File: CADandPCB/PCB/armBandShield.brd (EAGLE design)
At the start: 22.5 x 54.6 mm, 25 parts, among them U1 MPU-9250

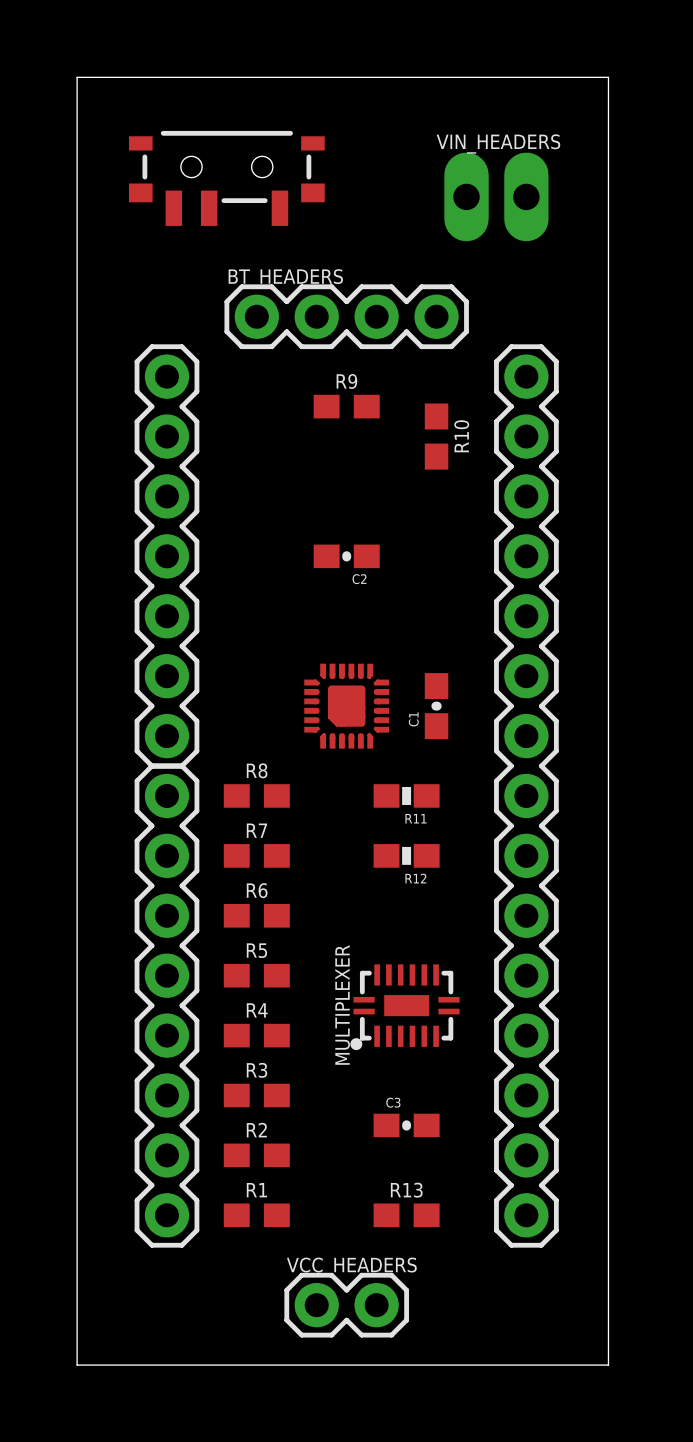
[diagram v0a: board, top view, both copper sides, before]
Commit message: Clean up silk screen and add ground plane.
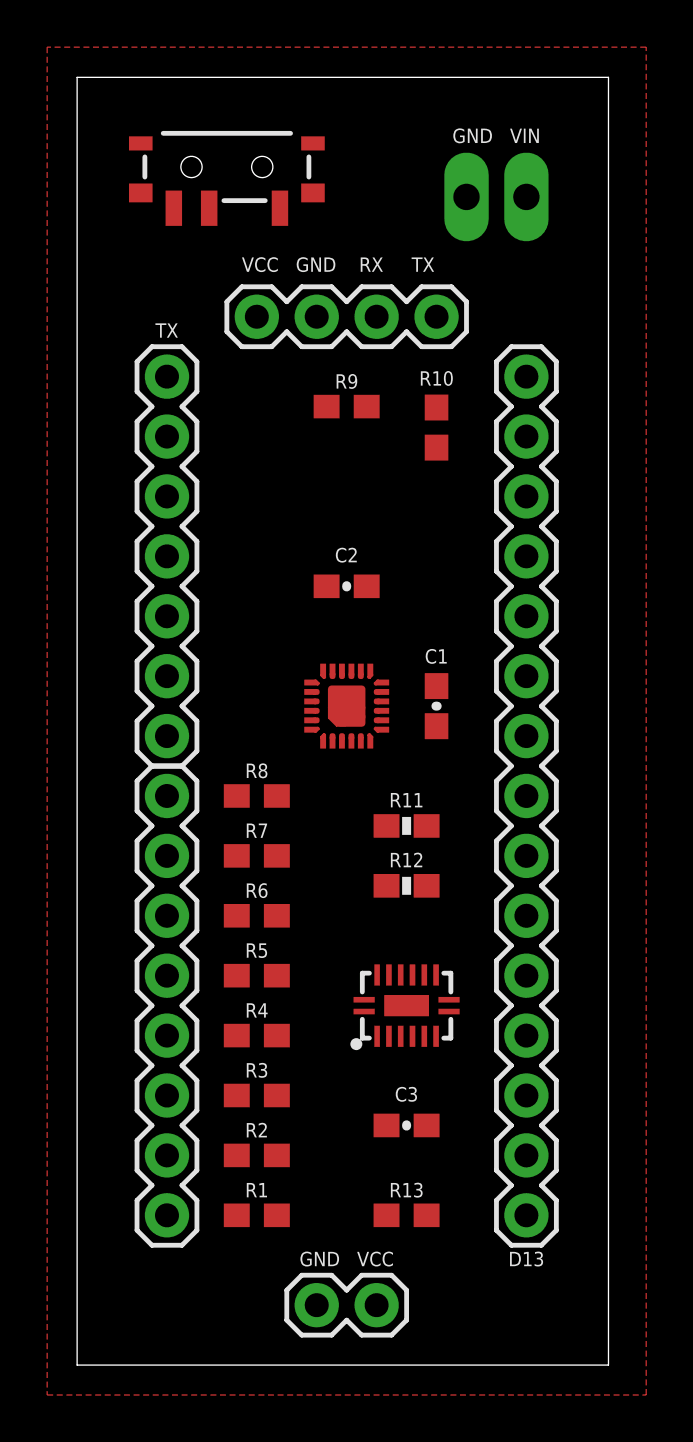
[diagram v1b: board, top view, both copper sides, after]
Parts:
- moved R11 1.27 mm to (14.0, 22.9)
- moved R12 1.27 mm to (14.0, 20.3)
- moved C2 1.27 mm to (11.4, 33.0)
- moved R10 0.38 mm to (15.2, 39.8)
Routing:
- added copper zone on layer 1, net GND
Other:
- board text added: "C2"
- board text added: "D13"
- board text added: "GND VCC"
- board text added: "GND VIN"
- board text added: "TX"
- board text added: "VCC GND RX TX"

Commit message: All connections routed
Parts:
- moved C1 5.39 mm to (11.4, 31.8), turned to 0 degrees
- moved R13 4.49 mm to (14.6, 10.8), turned to 270 degrees
- moved C2 4.20 mm to (7.62, 31.2), turned to 90 degrees
- moved R12 3.24 mm to (13.3, 23.5), turned to 270 degrees
- moved C3 3.24 mm to (14.6, 6.99), turned to 90 degrees
- moved R11 1.42 mm to (15.2, 23.5), turned to 270 degrees
- moved R8 1.09 mm to (6.73, 24.8), turned to 270 degrees
- moved MULTIPLEXER 0.38 mm to (13.6, 15.2)
- turned U1 to 180 degrees
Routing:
- net VCC: track 0.00 -> 61.8 mm, vias 0 -> 2
- net VCC_2: track 0.00 -> 47.8 mm, vias 0 -> 2
- net D2: track 0.00 -> 19.6 mm, vias 0 -> 1
- net D4: track 0.00 -> 18.4 mm, vias 0 -> 1
- net D3: track 0.00 -> 18.0 mm, vias 0 -> 1
- net FSR5: track 0.00 -> 17.1 mm, vias 0 -> 1
- net VIN: track 0.00 -> 17.0 mm
- net FSR1: track 0.00 -> 16.4 mm, vias 0 -> 1
- net FSR8: track 0.00 -> 15.9 mm
- net FSR2: track 0.00 -> 13.6 mm, vias 0 -> 1
- net A4/SDA: track 0.00 -> 13.6 mm, vias 0 -> 2
- net FSR3: track 0.00 -> 13.2 mm
- net FSR7: track 0.00 -> 11.8 mm
- net GND: track 0.00 -> 11.6 mm
- net RX: track 0.00 -> 11.0 mm
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- added copper zone on layer 16, net GND
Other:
- board size 22.5 x 54.6 mm -> 22.9 x 54.6 mm
- board text added: "BOURK AND RICO V1.0"
- board text added: "VIN GND"
- board text removed: "GND VIN"

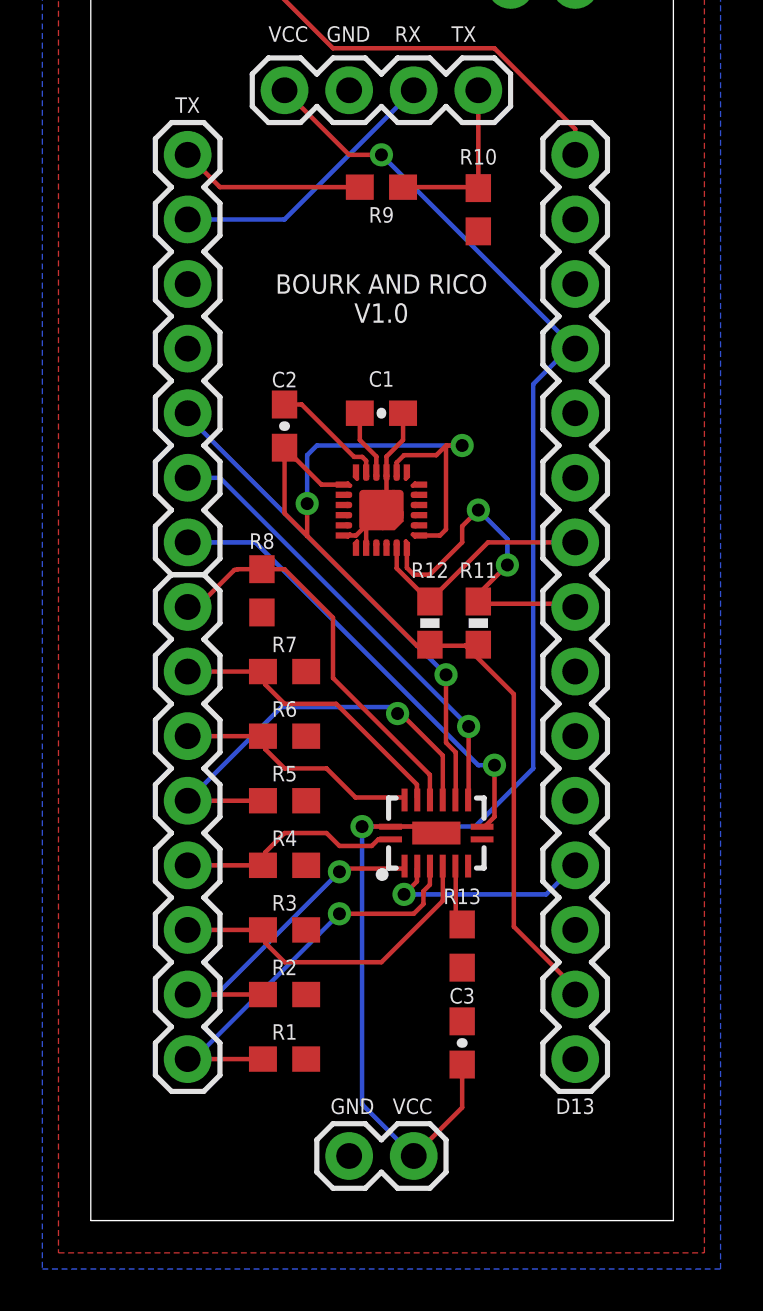
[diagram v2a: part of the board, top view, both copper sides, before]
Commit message: Increase solder pad lengths for chips
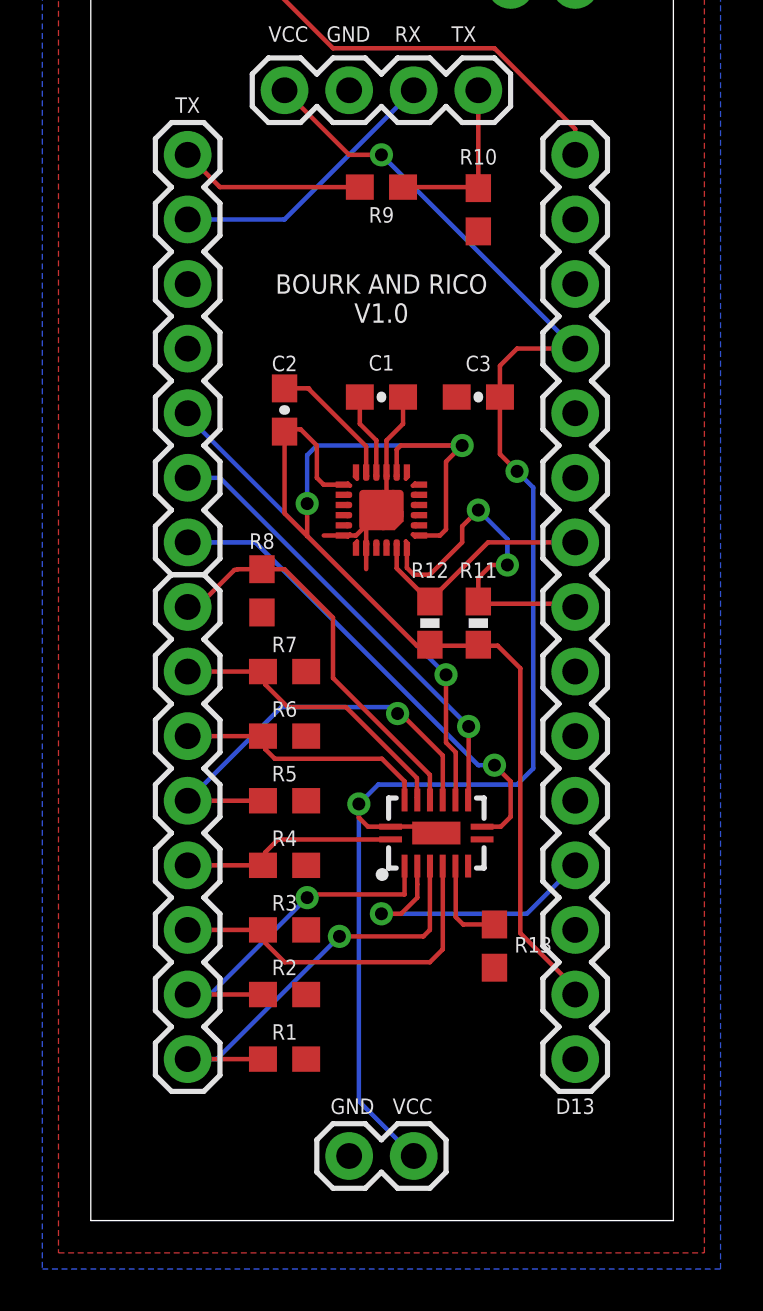
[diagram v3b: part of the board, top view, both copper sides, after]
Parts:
- moved C3 25.4 mm to (15.2, 32.4), turned to 180 degrees
- moved R13 1.27 mm to (15.9, 10.8)
- moved C1 0.63 mm to (11.4, 32.4)
- moved C2 0.63 mm to (7.62, 31.9)
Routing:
- net A0: track 8.53 -> 11.3 mm
- net GND: track 11.6 -> 14.4 mm
- net VCC_2: track 47.8 -> 50.5 mm
- net N$2: track 2.40 -> 3.65 mm
- net FSR3: track 13.2 -> 14.3 mm
- net D4: track 18.4 -> 19.3 mm
- net FSR1: track 16.4 -> 17.1 mm
- net REGOUT: track 2.53 -> 3.16 mm
- net FSR2: track 13.6 -> 14.2 mm
- net VCC: track 61.8 -> 61.3 mm, vias 2 -> 3

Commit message: Begin performing DRC checks
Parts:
- moved R13 3.30 mm to (15.0, 7.62), turned to 0 degrees
- moved R1 0.63 mm to (6.99, 6.35)
- moved R2 0.63 mm to (6.99, 8.89)
- moved R3 0.63 mm to (6.99, 11.4)
- moved R4 0.63 mm to (6.99, 14.0)
- moved R5 0.63 mm to (6.99, 16.5)
- moved R6 0.63 mm to (6.99, 19.1)
- moved R7 0.63 mm to (6.99, 21.6)
- moved R12 0.13 mm to (13.2, 23.5)
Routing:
- net N$2: track 3.65 -> 6.41 mm
- net FSR3: track 14.3 -> 15.6 mm
- net FSR2: track 14.2 -> 13.5 mm
- net D3: track 18.0 -> 18.7 mm
- net FSR5: track 17.1 -> 16.4 mm
- net FSR1: track 17.1 -> 16.5 mm
- net VCC_2: track 50.5 -> 51.1 mm
- net FSR8: track 15.9 -> 15.3 mm
- net GND: track 14.4 -> 14.3 mm, vias 0 -> 5

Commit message: Rev 1 board completed. Performed checks and added headers for switch.
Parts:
- removed VIN_SWITCH: (no value), SparkFun-Switches:SWITCH_SPST_SMD_A
- added SWITCH_HEADERS: 455-1750-1-ND, SparkFun-Connectors:1X03
- moved VIN_HEADERS 12.7 mm to (3.81, 50.2)
- moved R8 0.28 mm to (6.99, 24.9)
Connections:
- net N$1: now also SWITCH_HEADERS.2; no longer VIN_SWITCH.3
- net VIN: now also SWITCH_HEADERS.1; no longer VIN_SWITCH.2
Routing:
- net VIN: track 17.0 -> 8.26 mm
- net N$1: track 8.45 -> 16.6 mm
- net FSR1: track 16.5 -> 18.8 mm
- net FSR2: track 13.5 -> 15.4 mm
- net VCC: track 61.3 -> 62.8 mm
- net FSR4: track 8.70 -> 9.26 mm
- net FSR6: track 10.00 -> 10.5 mm
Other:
- board text added: "OFF ON"

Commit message: Replace MPU-9250 with MPU-6050. Added logic level. Cleaned up schematic.
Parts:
- removed C1, C2: 0.1uF, SparkFun-Capacitors:0603-CAP
- removed R11, R12: 10K, SparkFun-Resistors:0603-RES
- removed R13: 10k, SparkFun-Resistors:0603
- removed U1: MPU-9250, Testing:QFN24_PAD
- added C4, C7: 0.1uF, SparkFun-Capacitors:0603-CAP
- added C5: 10nF, SparkFun-Capacitors:0603
- added C6: 2.2nF, SparkFun-Capacitors:0603
- added IMU: MPU-6050-1, Testing:QFN-24-4MM2
- added LLC1, LLC2: BSS138, SparkFun:SOT23-3
- added R16, R17, R20, R21: 10K, SparkFun:0603-RES
- added R18, R19: 10K, SparkFun-Resistors:0603-RES
- MULTIPLEXER: value (none) -> 74HC4051
- renumbered MULTIPLEXER_HEADERS to FSR_HEADERS
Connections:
- removed net A4/SDA: R11.1, RIGHT_HEADER.8, U1.24
- removed net A5/SCL: R12.1, RIGHT_HEADER.9, U1.23
- removed net N$2: MULTIPLEXER.6, R13.1
- removed net REGOUT: C1.1, U1.10
- new net A4/SDA/HIGH: LLC1.3, R17.2, RIGHT_HEADER.8
- new net A4/SDA/LOW: IMU.24, LLC1.2, R16.2, R18.2
- new net A5/SCL/HIGH: LLC2.3, R21.2, RIGHT_HEADER.9
- new net A5/SCL/LOW: IMU.23, LLC2.2, R19.2, R20.2
- new net N$3: C6.1, IMU.20
- new net N$5: C4.1, IMU.10
- net GND: now also C4.2, C5.2, C6.2, C7.2, IMU.1, IMU.11, IMU.18, IMU.9, MULTIPLEXER.6; no longer C1.2, C2.2, R13.2, U1.11, U1.18, U1.20, U1.9, U1.CENTER
- net VCC: now also R17.1, R21.1
- net VCC_2: now also C5.1, C7.1, IMU.13, IMU.8, LLC1.1, LLC2.1, R16.1, R18.1, R19.1, R20.1; no longer C2.1, R11.2, R12.2, U1.1, U1.13, U1.8
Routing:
- net A4/SDA: track 13.9 -> 0.00 mm, vias 2 -> 0
- net A5/SCL: track 9.34 -> 0.00 mm
- net VCC_2: track 51.1 -> 41.8 mm
- net GND: track 14.3 -> 6.11 mm
- net N$2: track 6.41 -> 0.00 mm
- net REGOUT: track 3.16 -> 0.00 mm

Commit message: Initial layout 95% complete
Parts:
- removed FSR_HEADERS: (no value), SparkFun-Connectors:1X08
- removed IMU: MPU-6050-1, Testing:QFN-24-4MM2
- removed LLC1, LLC2: BSS138, SparkFun:SOT23-3
- removed MULTIPLEXER: 74HC4051, SparkFun-IC-Logic:DHVQFN-16-2.5X3.5MM
- added 74HC4051: U1, SparkFun-IC-Logic:DHVQFN-16-2.5X3.5MM
- added J1: FSR_HEADERS_1, SparkFun-Connectors:1X04
- added J2: FSR_HEADERS_2, SparkFun-Connectors:1X04
- added Q1, Q2: BSS138, SparkFun:SOT23-3
- added U2: MPU-6050-1, Testing:QFN-24-4MM2
- BT_HEADERS: value (none) -> J5; device SparkFun-Connectors:1X04@1 -> SparkFun-Connectors:1X04
- LEFT_HEADER: value (none) -> J3
- RIGHT_HEADER: value (none) -> J4; device SparkFun-Connectors:1X15 -> SparkFun-Connectors:1X14
- SWITCH_HEADERS: value 455-1750-1-ND -> J8
- VCC_HEADERS: value (none) -> J6; device SparkFun-Connectors:1X02 -> SparkFun-Connectors:1X02_LONGPADS
- VIN_HEADERS: value (none) -> J7
- moved C7 60.3 mm to (8.89, 32.4), turned to 270 degrees
- moved R20 58.1 mm to (10.8, 23.4), turned to 180 degrees
- moved R21 57.2 mm to (10.8, 16.5), turned to 90 degrees
- moved C4 56.5 mm to (10.2, 37.5), turned to 180 degrees
- moved R19 56.3 mm to (10.8, 25.7)
- moved C6 55.9 mm to (10.8, 27.9), turned to 180 degrees
- moved R18 51.6 mm to (15.2, 25.7), turned to 180 degrees
- moved C5 42.9 mm to (15.9, 37.5), turned to 180 degrees
- moved R16 32.0 mm to (15.2, 23.4), turned to 180 degrees
- moved R17 31.8 mm to (15.2, 16.5), turned to 90 degrees
- moved R8 19.2 mm to (2.03, 6.35)
- moved R1 18.3 mm to (25.3, 6.35), turned to 90 degrees
- moved C3 16.3 mm to (5.08, 19.7)
- moved R2 16.0 mm to (22.7, 6.35), turned to 90 degrees
- moved R7 15.4 mm to (4.57, 6.35), turned to 90 degrees
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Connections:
- net A0: now also 74HC4051.3, RIGHT_HEADER.3; no longer MULTIPLEXER.3, RIGHT_HEADER.4
- net A4/SDA/HIGH: now also Q1.3, RIGHT_HEADER.7; no longer LLC1.3, RIGHT_HEADER.8
- net A4/SDA/LOW: now also Q1.2, U2.24; no longer IMU.24, LLC1.2
- net A5/SCL/HIGH: now also Q2.3, RIGHT_HEADER.8; no longer LLC2.3, RIGHT_HEADER.9
- net A5/SCL/LOW: now also Q2.2, U2.23; no longer IMU.23, LLC2.2
- net D2: now also 74HC4051.11; no longer MULTIPLEXER.11
- net D3: now also 74HC4051.10; no longer MULTIPLEXER.10
- net D4: now also 74HC4051.9; no longer MULTIPLEXER.9
- net FSR1: now also 74HC4051.4, J2.1; no longer FSR_HEADERS.1, MULTIPLEXER.4
- net FSR2: now also 74HC4051.2, J2.2; no longer FSR_HEADERS.2, MULTIPLEXER.2
- net FSR3: now also 74HC4051.5, J2.3; no longer FSR_HEADERS.3, MULTIPLEXER.5
- net FSR4: now also 74HC4051.1, J2.4; no longer FSR_HEADERS.4, MULTIPLEXER.1
- net FSR5: now also 74HC4051.12, J1.1; no longer FSR_HEADERS.5, MULTIPLEXER.12
- net FSR6: now also 74HC4051.15, J1.2; no longer FSR_HEADERS.6, MULTIPLEXER.15
- net FSR7: now also 74HC4051.14, J1.3; no longer FSR_HEADERS.7, MULTIPLEXER.14
- net FSR8: now also 74HC4051.13, J1.4; no longer FSR_HEADERS.8, MULTIPLEXER.13
- net GND: now also 74HC4051.6, 74HC4051.7, 74HC4051.8, RIGHT_HEADER.13, U2.1, U2.11, U2.18, U2.9; no longer IMU.1, IMU.11, IMU.18, IMU.9, MULTIPLEXER.6, MULTIPLEXER.7, MULTIPLEXER.8, RIGHT_HEADER.14
- net N$3: now also U2.20; no longer IMU.20
- net N$5: now also U2.10; no longer IMU.10
- net VCC: now also 74HC4051.16, 74HC4051.EP, RIGHT_HEADER.11; no longer MULTIPLEXER.16, MULTIPLEXER.EP, RIGHT_HEADER.12
- net VCC_2: now also Q1.1, Q2.1, RIGHT_HEADER.1, U2.13, U2.8; no longer IMU.13, IMU.8, LLC1.1, LLC2.1, RIGHT_HEADER.2
- net VIN: now also RIGHT_HEADER.14; no longer RIGHT_HEADER.15
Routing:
- net VCC: track 62.8 -> 105.9 mm, vias 3 -> 0
- net VCC_2: track 41.8 -> 71.7 mm, vias 2 -> 0
- net D2: track 19.6 -> 0.00 mm, vias 1 -> 0
- net A5/SCL/HIGH: track 0.00 -> 18.8 mm
- net A4/SDA/HIGH: track 0.00 -> 12.1 mm
- net A0: track 11.3 -> 0.00 mm, vias 1 -> 0
- net A5/SCL/LOW: track 0.00 -> 10.8 mm
- net FSR8: track 15.7 -> 5.32 mm
- net A4/SDA/LOW: track 0.00 -> 9.27 mm
- net FSR1: track 18.8 -> 27.0 mm
- net FSR2: track 15.4 -> 22.8 mm, vias 1 -> 0
- net FSR3: track 15.9 -> 22.5 mm, vias 0 -> 1
- net FSR4: track 9.26 -> 2.99 mm
- net GND: track 6.11 -> 0.00 mm, vias 5 -> 0
- net D4: track 19.3 -> 14.6 mm, vias 1 -> 0
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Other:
- board size 22.9 x 54.6 mm -> 27.4 x 55.9 mm
- board text added: "3.3 V"
- board text added: "RX"
- board text removed: "C2"

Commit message: Board V2 Completed.
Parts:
- moved C7 8.28 mm to (13.3, 39.4), turned to 0 degrees
- moved 74HC4051 7.80 mm to (12.1, 10.7)
- moved J1 6.48 mm to (3.17, 2.41), turned to 90 degrees
- moved R8 5.68 mm to (6.35, 10.0), turned to 0 degrees
- moved R5 5.14 mm to (6.35, 2.41), turned to 0 degrees
- moved VCC_HEADERS 2.29 mm to (10.2, 2.92)
- moved R7 2.11 mm to (6.35, 7.49), turned to 0 degrees
- moved C3 2.01 mm to (5.71, 21.6)
- moved R6 1.59 mm to (6.35, 4.95), turned to 0 degrees
- moved R3 1.27 mm to (18.9, 6.35)
- moved C5 1.27 mm to (17.1, 37.5), turned to 0 degrees
- moved J2 1.27 mm to (24.0, 2.54)
- moved R1 1.27 mm to (24.0, 6.35)
- moved R2 1.27 mm to (21.5, 6.35)
- moved R4 1.27 mm to (16.4, 6.35)
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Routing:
- net D2: track 0.00 -> 28.4 mm
- net VCC: track 105.9 -> 88.4 mm, vias 0 -> 1
- net GND: track 0.00 -> 14.1 mm, vias 0 -> 5
- net A0: track 0.00 -> 11.9 mm, vias 0 -> 1
- net FSR1: track 27.0 -> 17.0 mm, vias 1 -> 0
- net FSR2: track 22.8 -> 13.1 mm
- net D4: track 14.6 -> 21.9 mm
- net D3: track 17.7 -> 24.8 mm
- net FSR4: track 2.99 -> 9.78 mm
- net RX: track 12.9 -> 18.1 mm
- net FSR7: track 12.6 -> 8.59 mm
- net FSR3: track 22.5 -> 18.5 mm
- net VCC_2: track 71.7 -> 75.6 mm, vias 0 -> 2
- net FSR8: track 5.32 -> 9.02 mm
- net FSR5: track 19.6 -> 22.5 mm, vias 1 -> 0
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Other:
- board size 27.4 x 55.9 mm -> 26.1 x 55.9 mm
- board text added: "5.0 V"
- board text added: "A4/SDA"
- board text added: "A5/SCL"
- board text added: "GND"
- board text removed: "BOURK AND RICO V1.0"
- board text removed: "D13"
